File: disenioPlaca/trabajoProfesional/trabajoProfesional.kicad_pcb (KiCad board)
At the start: 2 copper layers, 20.6 x 17.1 mm, 47 parts, among them T1 MPMOS, U1 1501

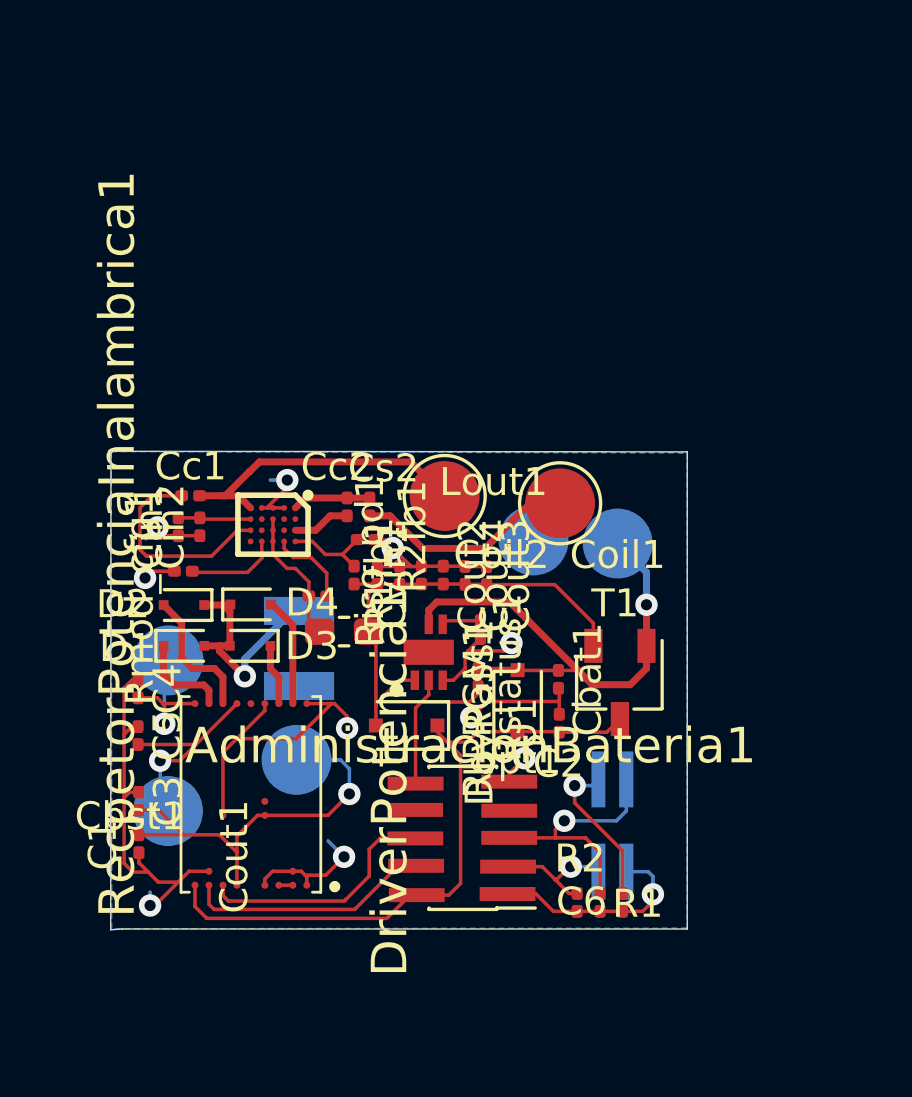
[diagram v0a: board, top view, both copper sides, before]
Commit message: se hacen mas gruesas las pistas y se rellenan las areas vacias de parte frontal
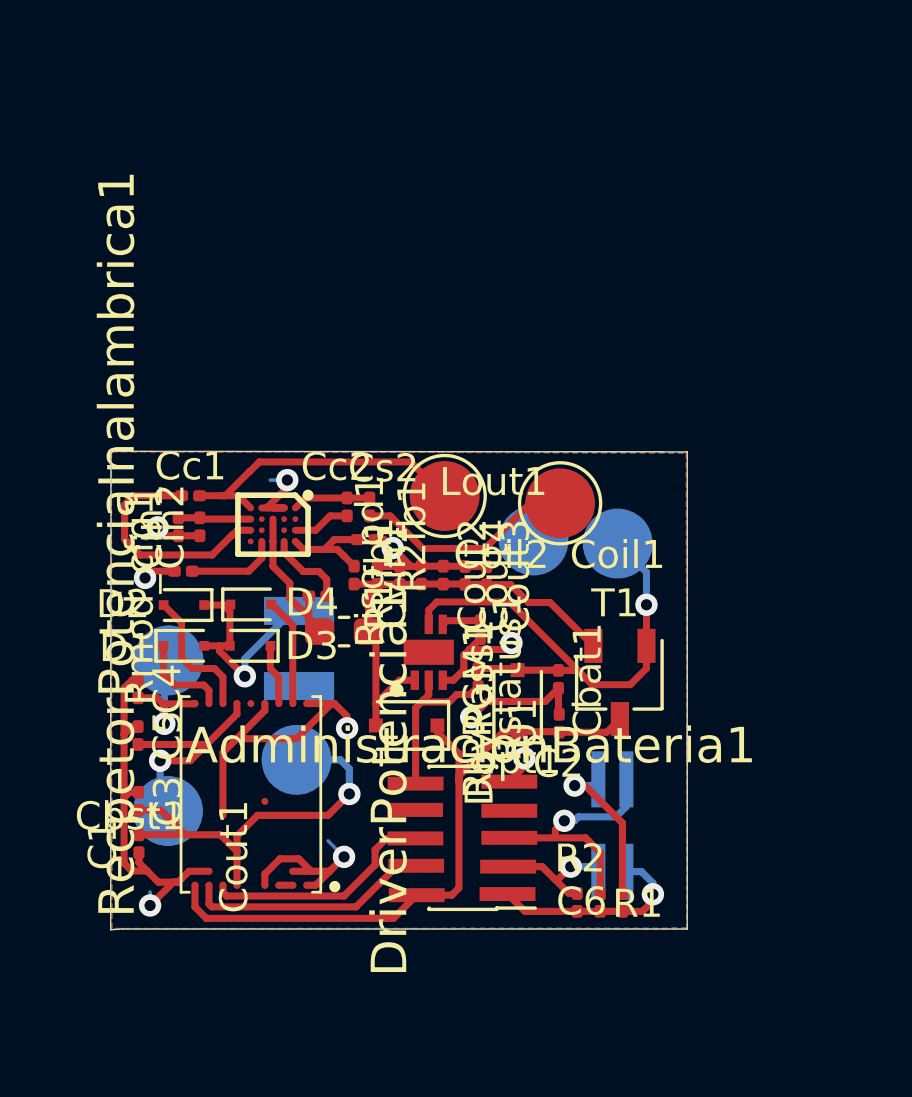
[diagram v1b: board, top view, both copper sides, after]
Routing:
- net GND: track 52.4 -> 64.1 mm
- net /Salida/Alimentacion: track 23.5 -> 31.3 mm
- net 10V: track 15.1 -> 20.8 mm
- net Net-(AdministracionBateria1-Pad1): track 17.0 -> 21.3 mm
- net SDAPresion: track 9.17 -> 11.8 mm
- net -HV: track 5.20 -> 7.33 mm
- net Net-(Cbst1-Pad1): track 4.35 -> 6.28 mm
- net SCLPresion: track 4.68 -> 5.86 mm
- net Net-(Cc1-Pad1): track 7.60 -> 8.52 mm
- net +HV: track 7.58 -> 8.17 mm
- net Net-(R1fb1-Pad2): track 3.22 -> 3.78 mm
- added copper zone on F.Cu, net (none)
